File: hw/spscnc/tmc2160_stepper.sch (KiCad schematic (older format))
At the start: 68 parts, among them IC1 TMC2160-TA, J4 8P8C_4xShielded, J8 8P8C_4xShielded, Q13 KIA50N06B, Q14 KIA50N06B, Q15 KIA50N06B, Q5 KIA50N06B, Q6 KIA50N06B, Q7 KIA50N06B, Q8 KIA50N06B, Q9 KIA50N06B

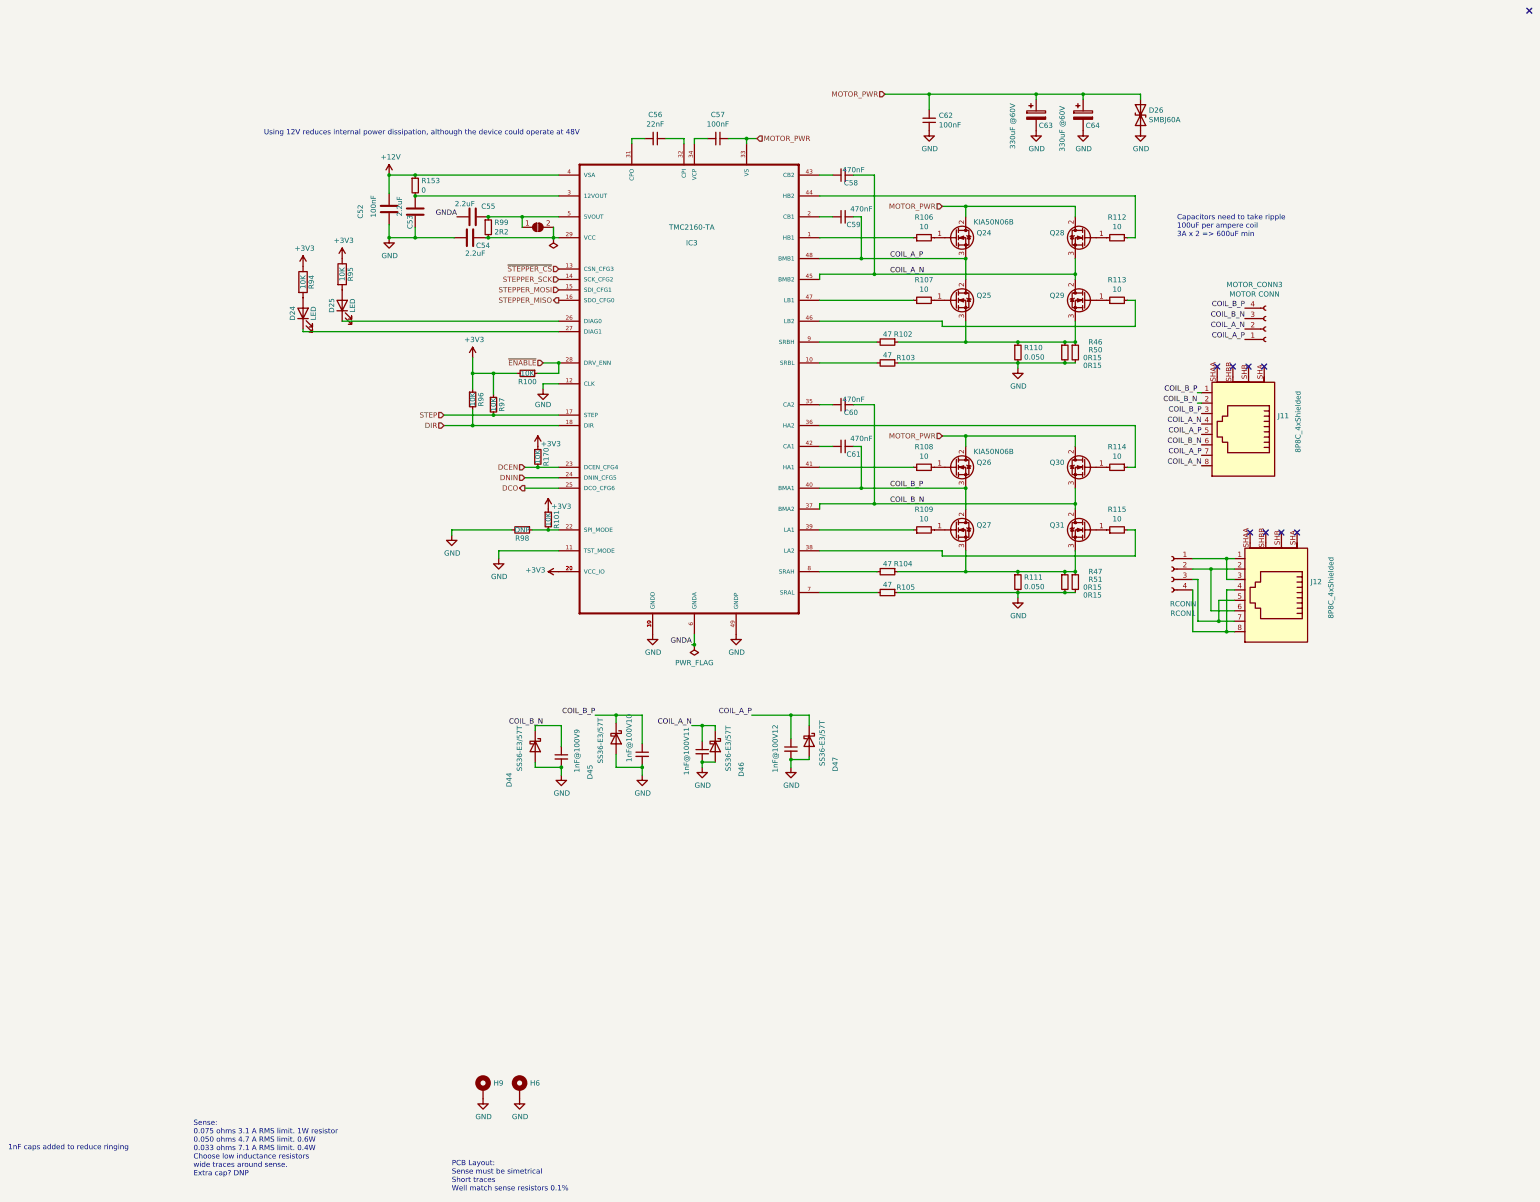
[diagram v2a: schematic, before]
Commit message: added most corrections on the schematic for i2s operation.
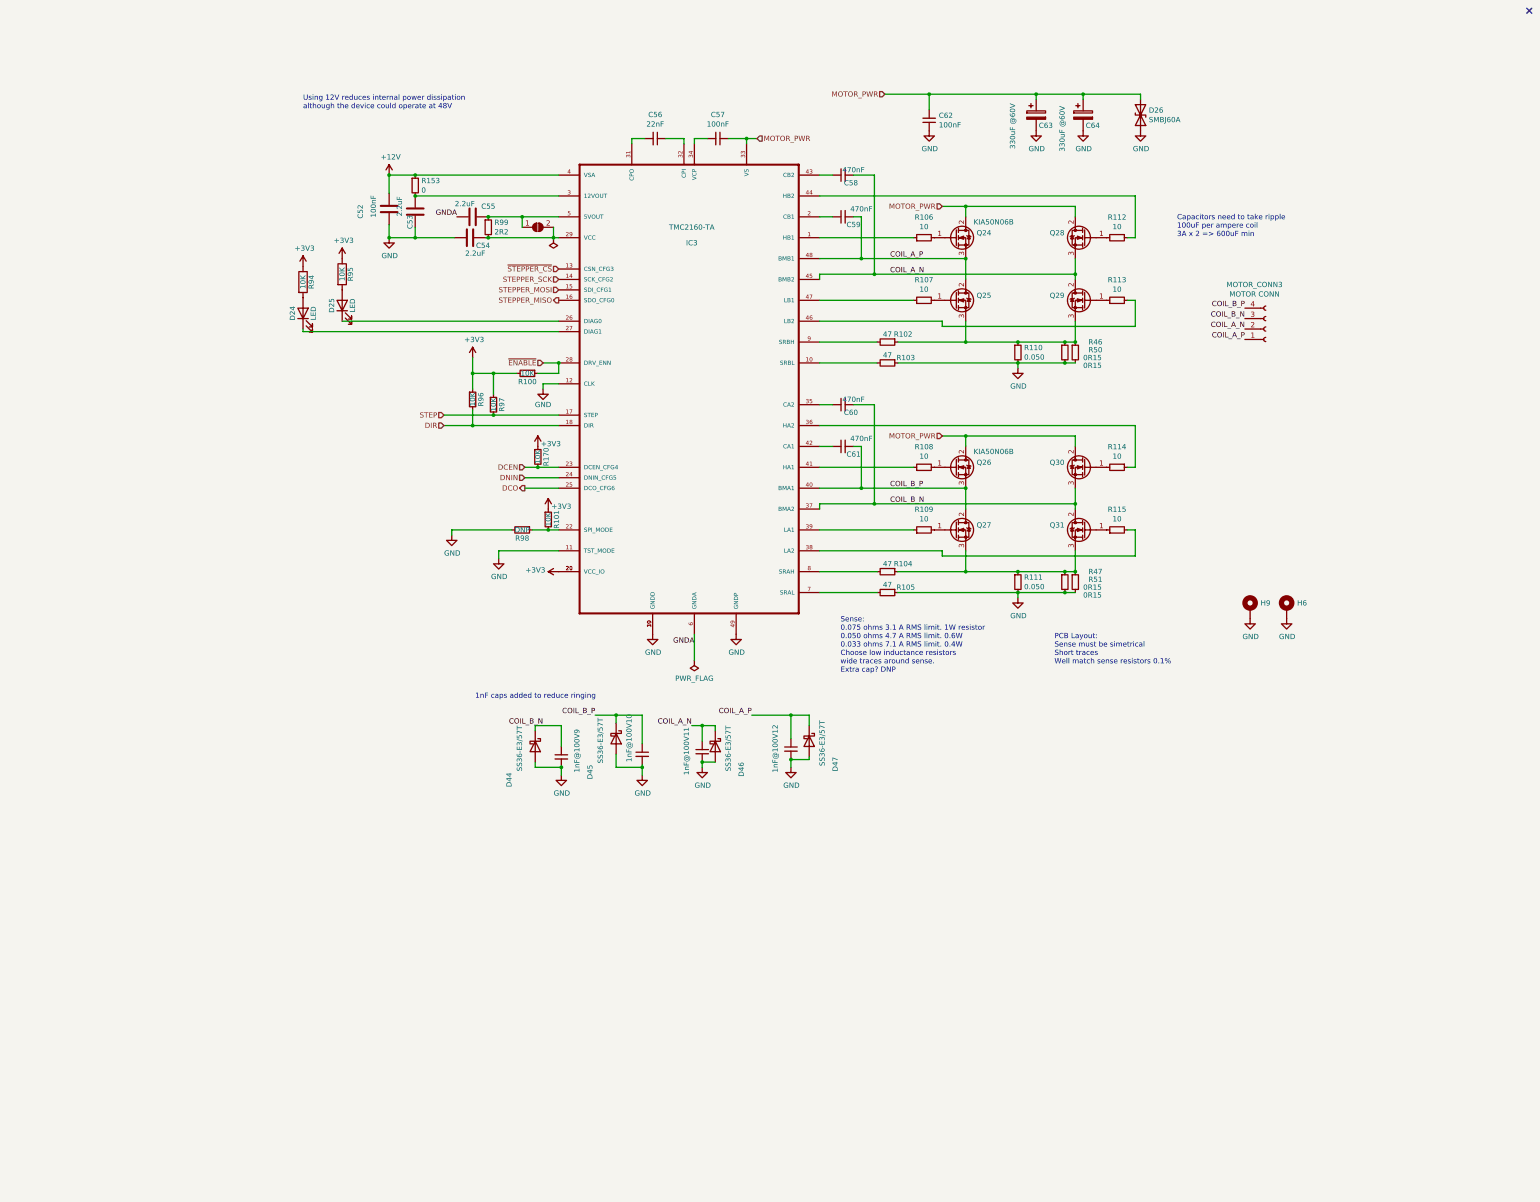
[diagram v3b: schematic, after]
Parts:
- removed J4, J8: 8P8C_4xShielded, industrial000:rj45_R-RJ45S08P-B000_C386763, symbol industrial:8P8C_4xShielded
- removed RCON1: RCONN, Connector_Phoenix_MSTB:PhoenixContact_MSTBV_2,5_4-GF-5,08_1x04_P5.08mm_Vertical_ThreadedFlange_MountHole, symbol Connector:Conn_01x04_Female
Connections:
- no-connect marks 9 -> 1
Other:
- note added: "Using 12V reduces internal power dissipation\nalthough the device could operate at 48V\n"
- note removed: "Using 12V reduces internal power dissipation, although the device could operate at 48V\n"
- moved on the sheet: H6, H9
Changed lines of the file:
@@
 $Descr A4 11693 8268
 encoding utf-8
-Sheet 12 16
+Sheet 12 17
 Title "Trinamic FluidNC CNC Controller"
 Date "2022-01-27"
@@
 	1    0    0    -1
 $EndComp
-Text Notes 675  1100 0    50   ~ 0
-Using 12V reduces internal power dissipation, although the device could operate at 48V\n
+Text Notes 1050 850  0    50   ~ 0
+Using 12V reduces internal power dissipation\nalthough the device could operate at 48V\n
 $Comp
 L Device:R R?
@@
 Text HLabel 3175 4475 0    50   Output ~ 0
 DCO
-Text Notes 0    11075 0    50   ~ 0
+Text Notes 6200 6250 0    50   ~ 0
 Sense:\n0.075 ohms 3.1 A RMS limit. 1W resistor\n0.050 ohms 4.7 A RMS limit. 0.6W\n0.033 ohms 7.1 A RMS limit. 0.4W\nChoose low inductance resistors\nwide traces around sense.\nExtra cap? DNP
-Text Notes 2475 11300 0    50   ~ 0
+Text Notes 8250 6250 0    50   ~ 0
 PCB Layout:\nSense must be simetrical\nShort traces\nWell match sense resistors 0.1%\n\n
 $Comp
 L Mechanical:MountingHole_Pad H4
 U 1 1 61F4E61C
-P 3125 10225
+P 10475 5625
 AR Path="/61E601B6/61F4E61C" Ref="H4"  Part="1"
 AR Path="/6203D74D/61F4E61C" Ref="H5"  Part="1"
@@
 AR Path="/6203DFCF/61F4E61C" Ref="H7"  Part="1"
 AR Path="/6221509B/61F4E61C" Ref="H?"  Part="1"
-F 0 "H6" H 3225 10274 50  0000 L CNN
-F 1 "MountingHole_Pad" H 3225 10183 50  0001 L CNN
-F 2 "MountingHole:MountingHole_2.2mm_M2_Pad_Via" H 3125 10225 50  0001 C CNN
-F 3 "~" H 3125 10225 50  0001 C CNN
-F 4 "DNP003" H 3125 10225 50  0001 C CNN "jlcpcb"
-	1    3125 10225
+F 0 "H6" H 10575 5674 50  0000 L CNN
+F 1 "MountingHole_Pad" H 10575 5583 50  0001 L CNN
+F 2 "MountingHole:MountingHole_2.2mm_M2_Pad_Via" H 10475 5625 50  0001 C CNN
+F 3 "~" H 10475 5625 50  0001 C CNN
+F 4 "DNP003" H 10475 5625 50  0001 C CNN "jlcpcb"
+	1    10475 5625
 	1    0    0    -1
 $EndComp
@@
 L power:GND-power #PWR0125
 U 1 1 61F4F366
-P 3125 10325
+P 10475 5725
 AR Path="/61E601B6/61F4F366" Ref="#PWR0125"  Part="1"
 AR Path="/6203D74D/61F4F366" Ref="#PWR055"  Part="1"
@@
 AR Path="/61F4F366" Ref="#PWR0125"  Part="1"
 AR Path="/6221509B/61F4F366" Ref="#PWR?"  Part="1"
-F 0 "#PWR075" H 3125 10075 50  0001 C CNN
-F 1 "GND" H 3130 10152 50  0000 C CNN
-F 2 "" H 3125 10325 50  0001 C CNN
-F 3 "" H 3125 10325 50  0001 C CNN
-	1    3125 10325
+F 0 "#PWR075" H 10475 5475 50  0001 C CNN
+F 1 "GND" H 10480 5552 50  0000 C CNN
+F 2 "" H 10475 5725 50  0001 C CNN
+F 3 "" H 10475 5725 50  0001 C CNN
+	1    10475 5725
 	1    0    0    -1
 $EndComp
@@
 L Mechanical:MountingHole_Pad H3
 U 1 1 61FC28D3
-P 2775 10225
+P 10125 5625
 AR Path="/61E601B6/61FC28D3" Ref="H3"  Part="1"
 AR Path="/6203D74D/61FC28D3" Ref="H8"  Part="1"
@@
 AR Path="/6203DFCF/61FC28D3" Ref="H10"  Part="1"
 AR Path="/6221509B/61FC28D3" Ref="H?"  Part="1"
-F 0 "H9" H 2875 10274 50  0000 L CNN
-F 1 "MountingHole_Pad" H 2875 10183 50  0001 L CNN
-F 2 "MountingHole:MountingHole_2.2mm_M2_Pad_Via" H 2775 10225 50  0001 C CNN
-F 3 "~" H 2775 10225 50  0001 C CNN
-F 4 "DNP003" H 2775 10225 50  0001 C CNN "jlcpcb"
-	1    2775 10225
+F 0 "H9" H 10225 5674 50  0000 L CNN
+F 1 "MountingHole_Pad" H 10225 5583 50  0001 L CNN
+F 2 "MountingHole:MountingHole_2.2mm_M2_Pad_Via" H 10125 5625 50  0001 C CNN
+F 3 "~" H 10125 5625 50  0001 C CNN
+F 4 "DNP003" H 10125 5625 50  0001 C CNN "jlcpcb"
+	1    10125 5625
 	1    0    0    -1
 $EndComp
@@
 L power:GND-power #PWR03
 U 1 1 61FC2A3D
-P 2775 10325
+P 10125 5725
 AR Path="/61E601B6/61FC2A3D" Ref="#PWR03"  Part="1"
 AR Path="/6203D74D/61FC2A3D" Ref="#PWR04"  Part="1"
@@
 AR Path="/61FC2A3D" Ref="#PWR03"  Part="1"
 AR Path="/6221509B/61FC2A3D" Ref="#PWR?"  Part="1"
-F 0 "#PWR06" H 2775 10075 50  0001 C CNN
-F 1 "GND" H 2780 10152 50  0000 C CNN
-F 2 "" H 2775 10325 50  0001 C CNN
-F 3 "" H 2775 10325 50  0001 C CNN
-	1    2775 10325
-	1    0    0    -1
-$EndComp
-$Comp
-L industrial:8P8C_4xShielded J?
-U 1 1 61F14B50
-P 10060 3860
-AR Path="/61C80DFB/61F14B50" Ref="J?"  Part="1"
-AR Path="/61C80E48/61F14B50" Ref="J?"  Part="1"
-AR Path="/61C80E8F/61F14B50" Ref="J?"  Part="1"
-AR Path="/61CEF4C9/61F14B50" Ref="J?"  Part="1"
-AR Path="/61C80DCB/61F14B50" Ref="J?"  Part="1"
-AR Path="/61DEDDC1/61F14B50" Ref="J?"  Part="1"
-AR Path="/61E601B6/61F14B50" Ref="J4"  Part="1"
-AR Path="/6203D74D/61F14B50" Ref="J9"  Part="1"
-AR Path="/6203DA5D/61F14B50" Ref="J11"  Part="1"
-AR Path="/6203DFCF/61F14B50" Ref="J13"  Part="1"
-AR Path="/6221509B/61F14B50" Ref="J?"  Part="1"
-F 0 "J11" H 9730 3782 50  0000 R CNN
-F 1 "8P8C_4xShielded" V 9535 4135 50  0000 R CNN
-F 2 "industrial000:rj45_R-RJ45S08P-B000_C386763" V 10060 3885 50  0001 C CNN
-F 3 "~" V 10060 3885 50  0001 C CNN
-F 4 "DNP007" H 10060 3860 50  0001 C CNN "jlcpcb"
-	1    10060 3860
-	-1   0    0    1
-$EndComp
-Text Label 9620 3560 2    50   ~ 0
-COIL_B_P
-Wire Wire Line
-	9660 3560 9620 3560
-Text Label 9620 3660 2    50   ~ 0
-COIL_B_N
-Wire Wire Line
-	9620 3660 9660 3660
-Text Label 9660 3760 2    50   ~ 0
-COIL_B_P
-Text Label 9660 4060 2    50   ~ 0
-COIL_B_N
-Text Label 9660 3860 2    50   ~ 0
-COIL_A_N
-Text Label 9660 3960 2    50   ~ 0
-COIL_A_P
-Text Label 9660 4160 2    50   ~ 0
-COIL_A_P
-Text Label 9660 4260 2    50   ~ 0
-COIL_A_N
-NoConn ~ 9810 3310
-NoConn ~ 9960 3310
-NoConn ~ 10110 3310
-NoConn ~ 10260 3310
-$Comp
-L industrial:8P8C_4xShielded J?
-U 1 1 61F559AD
-P 10375 5450
-AR Path="/61C80DFB/61F559AD" Ref="J?"  Part="1"
-AR Path="/61C80E48/61F559AD" Ref="J?"  Part="1"
-AR Path="/61C80E8F/61F559AD" Ref="J?"  Part="1"
-AR Path="/61CEF4C9/61F559AD" Ref="J?"  Part="1"
-AR Path="/61C80DCB/61F559AD" Ref="J?"  Part="1"
-AR Path="/61DEDDC1/61F559AD" Ref="J?"  Part="1"
-AR Path="/61E601B6/61F559AD" Ref="J8"  Part="1"
-AR Path="/6203D74D/61F559AD" Ref="J10"  Part="1"
-AR Path="/6203DA5D/61F559AD" Ref="J12"  Part="1"
-AR Path="/6203DFCF/61F559AD" Ref="J14"  Part="1"
-AR Path="/6221509B/61F559AD" Ref="J?"  Part="1"
-F 0 "J12" H 10045 5372 50  0000 R CNN
-F 1 "8P8C_4xShielded" V 9850 5725 50  0000 R CNN
-F 2 "industrial000:rj45_R-RJ45S08P-B000_C386763" V 10375 5475 50  0001 C CNN
-F 3 "~" V 10375 5475 50  0001 C CNN
-F 4 "DNP007" H 10375 5450 50  0001 C CNN "jlcpcb"
-	1    10375 5450
-	-1   0    0    1
-$EndComp
-NoConn ~ 10125 4900
-NoConn ~ 10275 4900
-NoConn ~ 10425 4900
-NoConn ~ 10575 4900
-$Comp
-L Connector:Conn_01x04_Female MOTOR_CONN?
-U 1 1 61F5C974
-P 9375 5250
-AR Path="/61E0961E/61F5C974" Ref="MOTOR_CONN?"  Part="1"
-AR Path="/61C743E7/61AF0AE8/61F5C974" Ref="MOTOR_CONN?"  Part="1"
-AR Path="/61E601B6/61F5C974" Ref="RCON1"  Part="1"
-AR Path="/6203D74D/61F5C974" Ref="MOTOR_CONN5"  Part="1"
-AR Path="/6203DA5D/61F5C974" Ref="MOTOR_CONN6"  Part="1"
-AR Path="/6203DFCF/61F5C974" Ref="MOTOR_CONN7"  Part="1"
-AR Path="/6221509B/61F5C974" Ref="RCON?"  Part="1"
-F 0 "RCON1" H 9267 4825 50  0000 C CNN
-F 1 "RCONN" H 9267 4916 50  0000 C CNN
-F 2 "Connector_Phoenix_MSTB:PhoenixContact_MSTBV_2,5_4-GF-5,08_1x04_P5.08mm_Vertical_ThreadedFlange_MountHole" H 9375 5250 50  0001 C CNN
-F 3 "~" H 9375 5250 50  0001 C CNN
-F 4 "DNP018" H 9375 5250 50  0001 C CNN "jlcpcb"
-	1    9375 5250
-	-1   0    0    -1
-$EndComp
-Wire Wire Line
-	9975 5150 9900 5150
-Wire Wire Line
-	9575 5250 9750 5250
-Wire Wire Line
-	9975 5850 9900 5850
-Wire Wire Line
-	9575 5850 9575 5450
-Wire Wire Line
-	9575 5350 9625 5350
-Wire Wire Line
-	9625 5350 9625 5750
-Wire Wire Line
-	9625 5750 9825 5750
-Wire Wire Line
-	9975 5350 9900 5350
-Wire Wire Line
-	9900 5350 9900 5150
-Connection ~ 9900 5150
-Wire Wire Line
-	9900 5150 9575 5150
-Wire Wire Line
-	9975 5650 9750 5650
-Wire Wire Line
-	9750 5650 9750 5250
-Connection ~ 9750 5250
-Wire Wire Line
-	9750 5250 9975 5250
-Wire Wire Line
-	9975 5450 9900 5450
-Wire Wire Line
-	9900 5450 9900 5850
-Connection ~ 9900 5850
-Wire Wire Line
-	9900 5850 9575 5850
-Wire Wire Line
-	9975 5550 9825 5550
-Wire Wire Line
-	9825 5550 9825 5750
-Connection ~ 9825 5750
-Wire Wire Line
-	9825 5750 9975 5750
+F 0 "#PWR06" H 10125 5475 50  0001 C CNN
+F 1 "GND" H 10130 5552 50  0000 C CNN
+F 2 "" H 10125 5725 50  0001 C CNN
+F 3 "" H 10125 5725 50  0001 C CNN
+	1    10125 5725
+	1    0    0    -1
+$EndComp
 $Comp
 L Device:R_Small R?
@@
 Wire Wire Line
 	4300 6650 4300 6925
-Text Notes -1775 10825 0    50   ~ 0
+Text Notes 2700 6500 0    50   ~ 0
 1nF caps added to reduce ringing
 $Comp
@@
 Text Label 2525 1875 2    50   ~ 0
 GNDA
-Text Label 4775 5975 2    50   ~ 0
+Text Label 4800 5975 2    50   ~ 0
 GNDA
-Wire Wire Line
-	4775 5975 4800 5975
-Wire Wire Line
-	4800 5975 4800 5875
 Wire Wire Line
 	2125 1975 2125 2075
@@
 L power:PWR_FLAG-power #FLG0104
 U 1 1 61F8983B
-P 4800 5975
+P 4800 6125
 AR Path="/61E601B6/61F8983B" Ref="#FLG0104"  Part="1"
 AR Path="/6203D74D/61F8983B" Ref="#FLG0109"  Part="1"
@@
 AR Path="/61F8983B" Ref="#FLG0104"  Part="1"
 AR Path="/6221509B/61F8983B" Ref="#FLG?"  Part="1"
-F 0 "#FLG0115" H 4800 6050 50  0001 C CNN
-F 1 "PWR_FLAG" H 4800 6148 50  0000 C CNN
-F 2 "" H 4800 5975 50  0001 C CNN
-F 3 "~" H 4800 5975 50  0001 C CNN
-	1    4800 5975
+F 0 "#FLG0115" H 4800 6200 50  0001 C CNN
+F 1 "PWR_FLAG" H 4800 6298 50  0000 C CNN
+F 2 "" H 4800 6125 50  0001 C CNN
+F 3 "~" H 4800 6125 50  0001 C CNN
+	1    4800 6125
 	-1   0    0    1
 $EndComp
-Connection ~ 4800 5975
+Wire Wire Line
+	4800 6125 4800 5875
 $EndSCHEMATC
